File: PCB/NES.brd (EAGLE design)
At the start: 58.5 x 61 mm, 15 parts, among them U1 SN74AHCT125N, U2 SN74AHCT125N

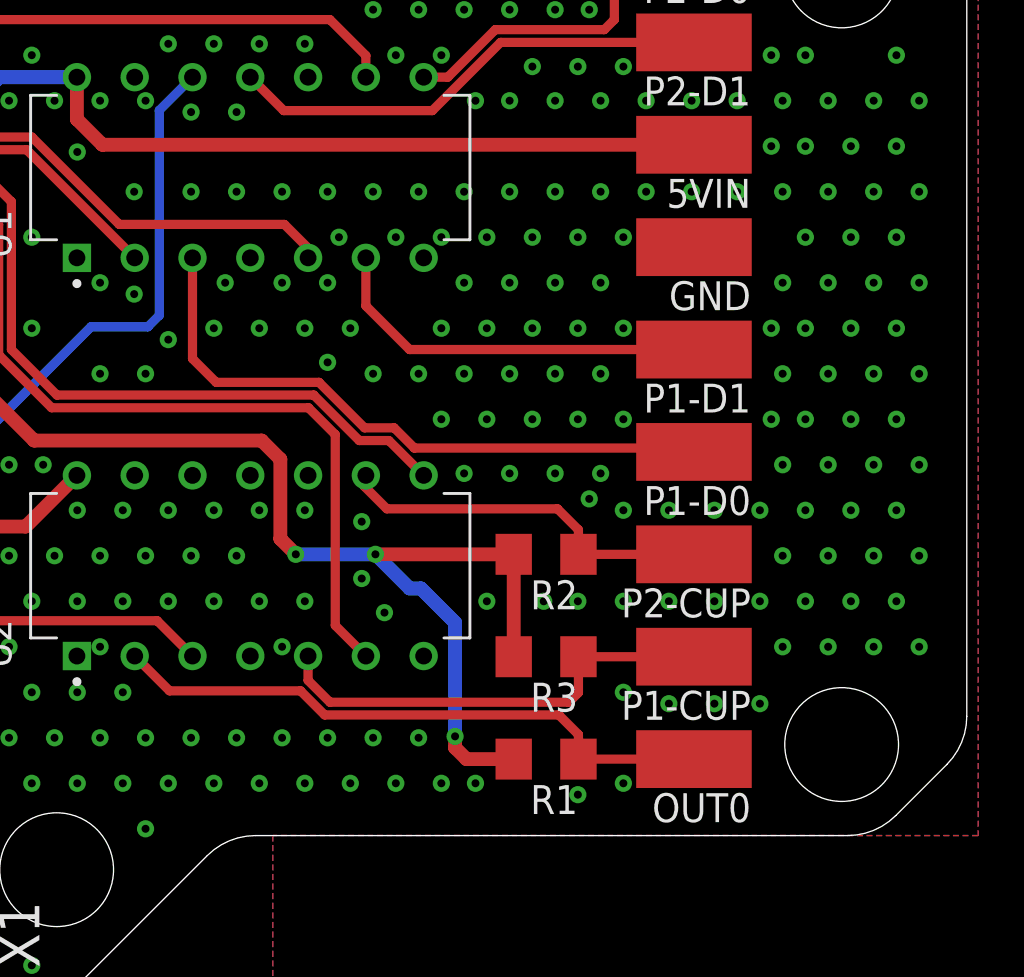
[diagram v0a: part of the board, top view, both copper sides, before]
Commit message: PCB Updates/New Additions
All existing PCBs had silkscreen updates and NES, Virtual Boy, PSX/PS2, Nintendo 64, Saturn have been added.
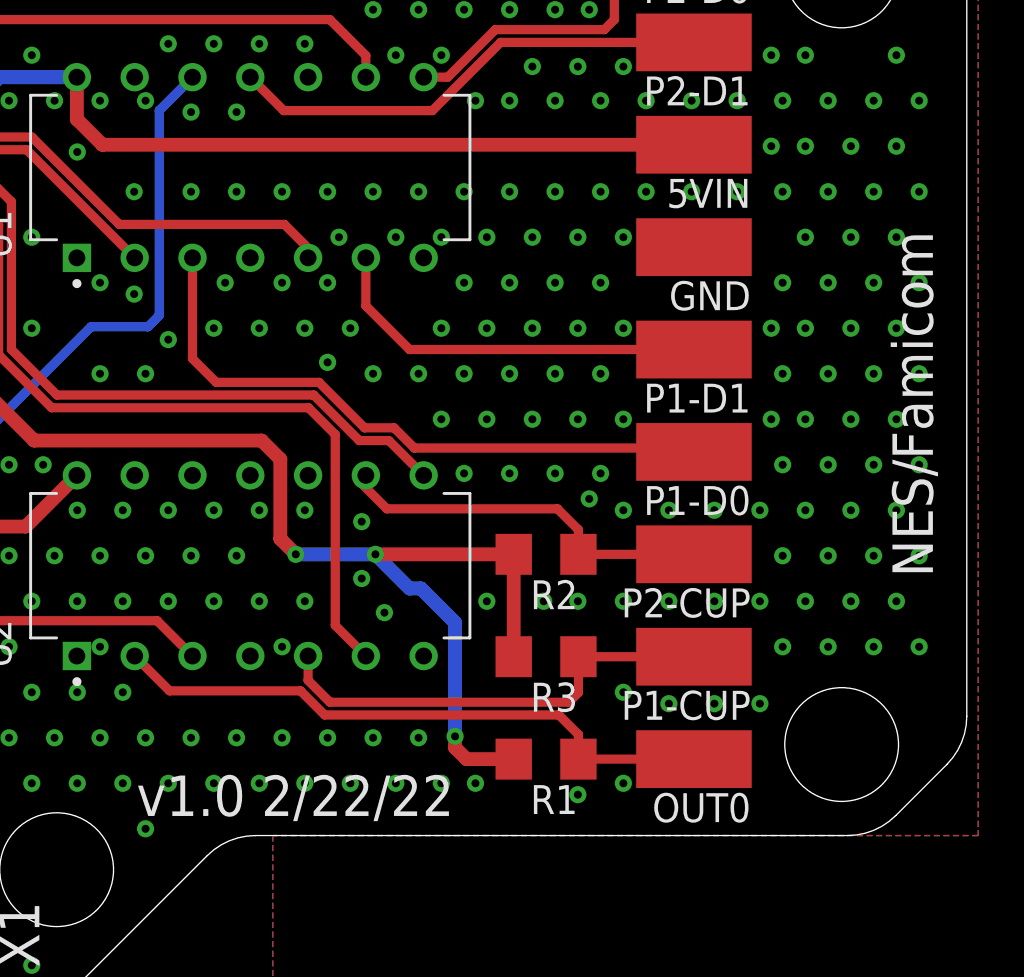
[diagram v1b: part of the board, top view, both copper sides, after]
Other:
- board text added: "NES/Famicom"
- board text added: "v1.0 2/22/22"
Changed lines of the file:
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@@
 <drawing>
 <settings>
-<setting alwaysvectorfont="yes"/>
+<setting alwaysvectorfont="no"/>
 <setting verticaltext="up"/>
 </settings>
@@
 <hole x="18.49" y="53.14" drill="5"/>
 <hole x="18.49" y="8.14" drill="5"/>
+<text x="57" y="21" size="1.778" layer="21" rot="R90">NES/Famicom</text>
+<text x="22" y="10.5" size="1.778" layer="21">v1.0 2/22/22</text>
 </plain>
 <attributes>
@@
 <element name="R1" library="adafruit" library_urn="urn:adsk.eagle:library:420" package="R1206" package3d_urn="urn:adsk.eagle:package:6240569/1" value="3.6K" x="40" y="13" smashed="yes" rot="R180">
 <attribute name="NAME" x="41.397" y="11.857" size="1.27" layer="25" rot="R180"/>
-<attribute name="VALUE" x="41.397" y="15.413" size="1.27" layer="27" rot="R180"/>
 </element>
 <element name="R2" library="adafruit" library_urn="urn:adsk.eagle:library:420" package="R1206" package3d_urn="urn:adsk.eagle:package:6240569/1" value="3.6K" x="40" y="22" smashed="yes" rot="R180">
 <attribute name="NAME" x="41.397" y="20.857" size="1.27" layer="25" rot="R180"/>
-<attribute name="VALUE" x="41.397" y="24.413" size="1.27" layer="27" rot="R180"/>
 </element>
 <element name="R3" library="adafruit" library_urn="urn:adsk.eagle:library:420" package="R1206" package3d_urn="urn:adsk.eagle:package:6240569/1" value="3.6K" x="40" y="17.5" smashed="yes" rot="R180">
 <attribute name="NAME" x="41.397" y="16.357" size="1.27" layer="25" rot="R180"/>
-<attribute name="VALUE" x="41.397" y="19.913" size="1.27" layer="27" rot="R180"/>
 </element>
 </elements>

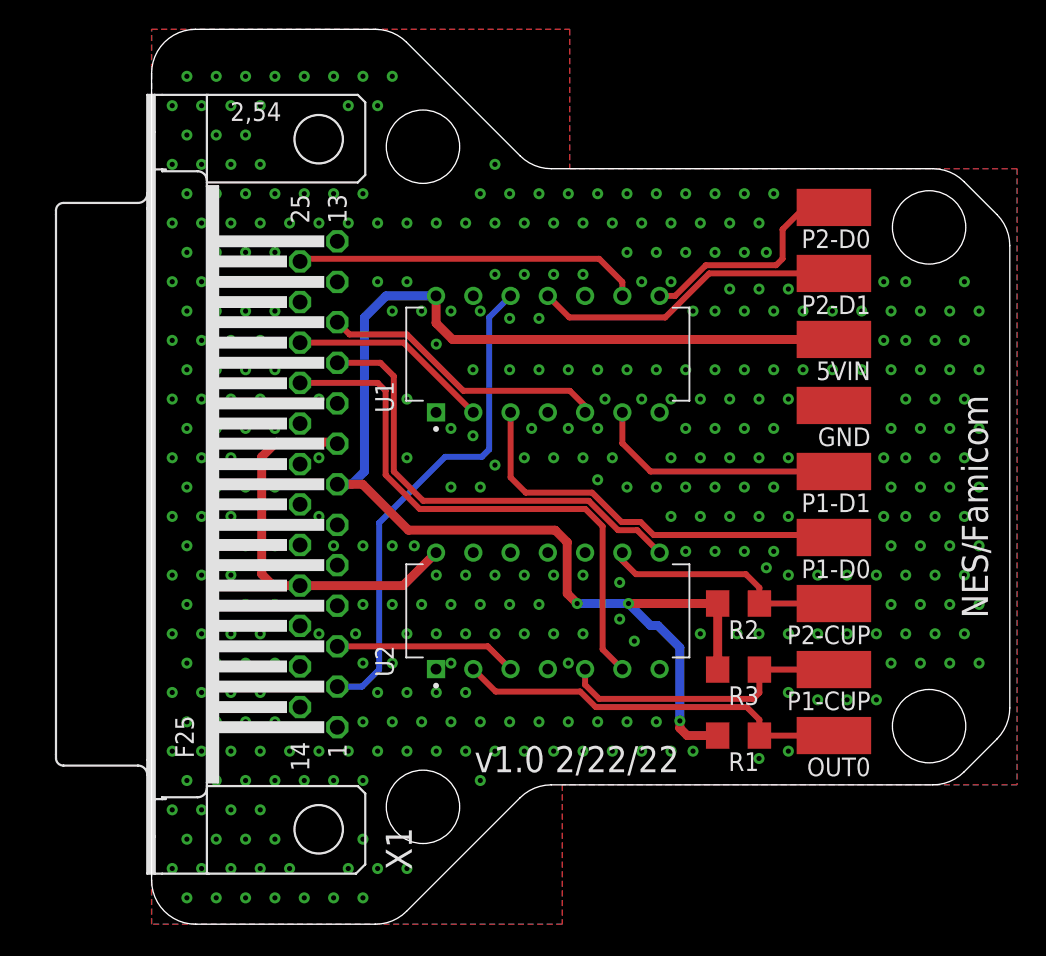
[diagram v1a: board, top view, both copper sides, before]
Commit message: PCB Update for better Housing Fit
All the PCBs were updated for better housing fitment.

Common Changes across all PCBs:
1. All Aux PCBs are now the exact same size.  (there was a .1mm-.5mm Variance previous)
2. All Aux PCBs Mounting holes are in the same location (there was a .05mm-.1mm Variance previous)
3. The DB25 has been moved 1.2mm close to the edge of the PCB for better connection when in the housing.

PCB Specific Updates:
3DO - Rename Pads (Removed trailing numbers), Flipped U2 to match U1, Moved U1 & U2 to same coordinates as other 2 Component PCBs in collection.

PCE & NES- Moved U1 & U2 to same coordinates as other 2 Component PCBs in collection.

PS2/PSX & Saturn - Added Notch on back edge of PCB for access for wires that need to attach to bottom layer of PCB.

All Gerbers have been updated.

New PCBs have been ordered for testing.
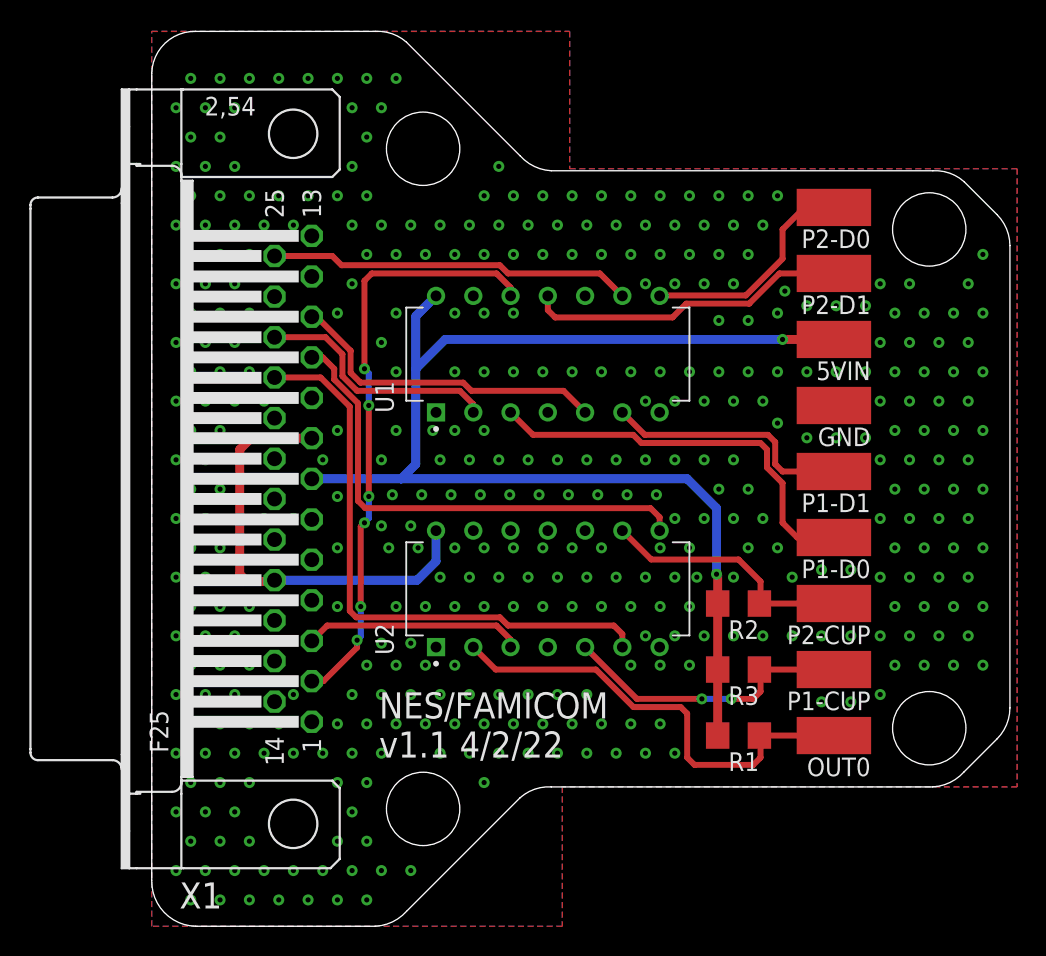
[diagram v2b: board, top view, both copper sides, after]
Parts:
- moved X1 1.78 mm to (9.64, 30.5)
- moved U2 1.50 mm to (27.0, 23.0)
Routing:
- net 5VIN: track 96.5 -> 86.7 mm, vias 3 -> 2
- net IO25: track 34.0 -> 40.6 mm, vias 0 -> 6
- net OUT0: track 27.1 -> 31.5 mm
- net 3V3IN: track 26.7 -> 30.0 mm
- net IO19: track 13.8 -> 16.9 mm
- net IO21: track 19.7 -> 22.2 mm
- net IO32: track 12.5 -> 14.9 mm
- net IO18: track 31.1 -> 33.5 mm
- net IO5: track 38.3 -> 40.0 mm
- net IO22: track 23.6 -> 24.8 mm
- net P2-D1: track 21.4 -> 21.9 mm
- net P2-CUP: track 16.9 -> 17.4 mm
- net P1-CUP: vias 0 -> 2
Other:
- outline, holes or cut-outs redrawn
- board text added: "NES/FAMICOM v1.1 4/2/22"
- board text removed: "NES/Famicom"
- board text removed: "v1.0 2/22/22"

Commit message: Added exposed GND plane at DB25 anchors
All PCBs have been update to have exposed GND plane pads for the DB25 anchor points.

This resolves Issue 54
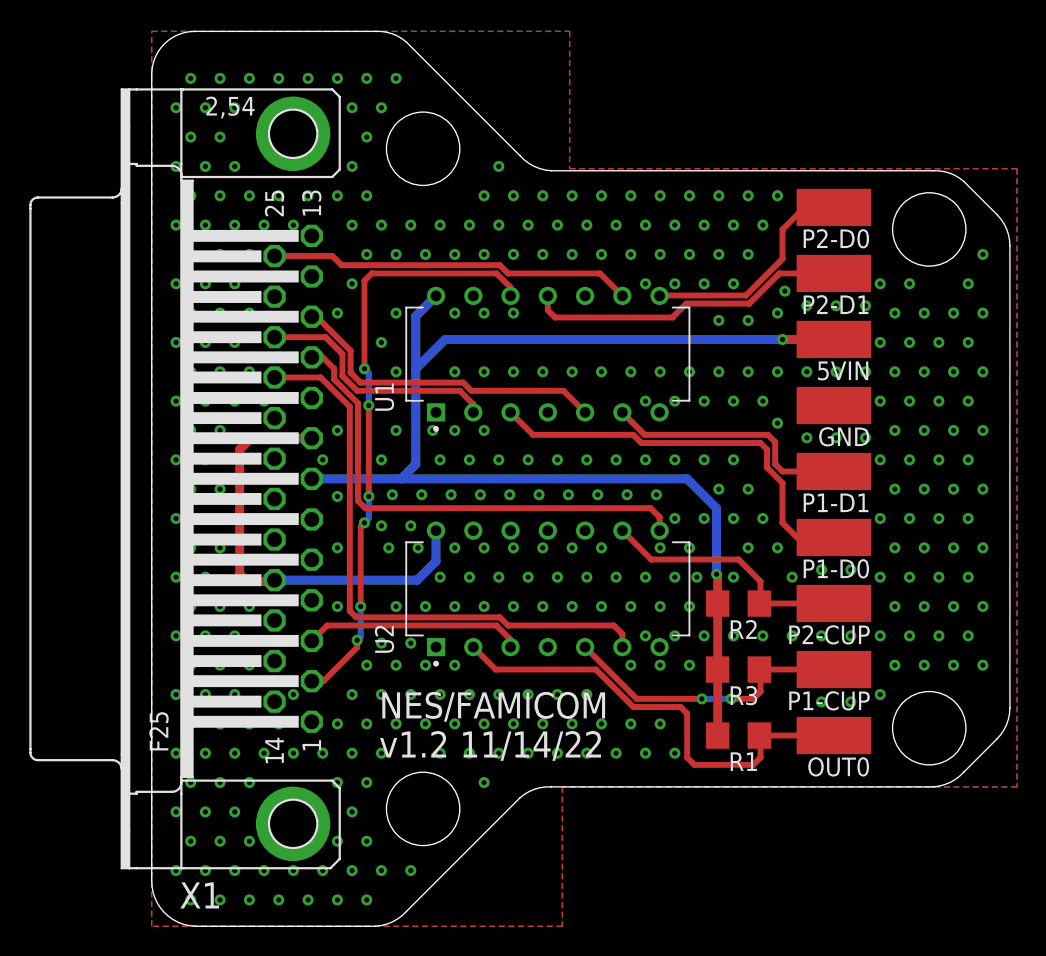
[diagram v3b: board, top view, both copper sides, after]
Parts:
- X1: device SparkFun-Retired:F25H -> SparkFun-Retired:F25HP
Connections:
- net GND: now also X1.GND1, X1.GND2
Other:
- board text added: "NES/FAMICOM v1.2 11/14/22"
- board text removed: "NES/FAMICOM v1.1 4/2/22"
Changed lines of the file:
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@@
 <hole x="18.5" y="8" drill="5"/>
 <text x="15.5" y="11.5" size="1.778" layer="21">NES/FAMICOM
-v1.1 4/2/22</text>
+v1.2 11/14/22</text>
 </plain>
 <attributes>
@@
 <attribute name="PURCHASE-URL" value="https://pricing.snapeda.com/search/part/SN74AHCT125N/?ref=eda" x="65.1" y="47.13" size="1.778" layer="27" rot="R90" display="off"/>
 </element>
-<element name="X1" library="SparkFun-Retired" package="F25H" value="" x="9.64" y="30.5" smashed="yes" rot="R90">
+<element name="X1" library="SparkFun-Retired" package="F25HP" value="" x="9.64" y="30.5" smashed="yes" rot="R90">
 <attribute name="NAME" x="4.789" y="2.99" size="1.778" layer="25" ratio="10" rot="R180"/>
 <attribute name="VALUE" x="-4.33" y="22.118" size="1.778" layer="27" ratio="10" rot="R90"/>
@@
 <via x="55.6568" y="43.7968" extent="1-16" drill="0.35"/>
 <via x="56.6568" y="45.7968" extent="1-16" drill="0.35"/>
+<contactref element="X1" pad="GND1"/>
+<contactref element="X1" pad="GND2"/>
 </signal>
 <signal name="5VIN">

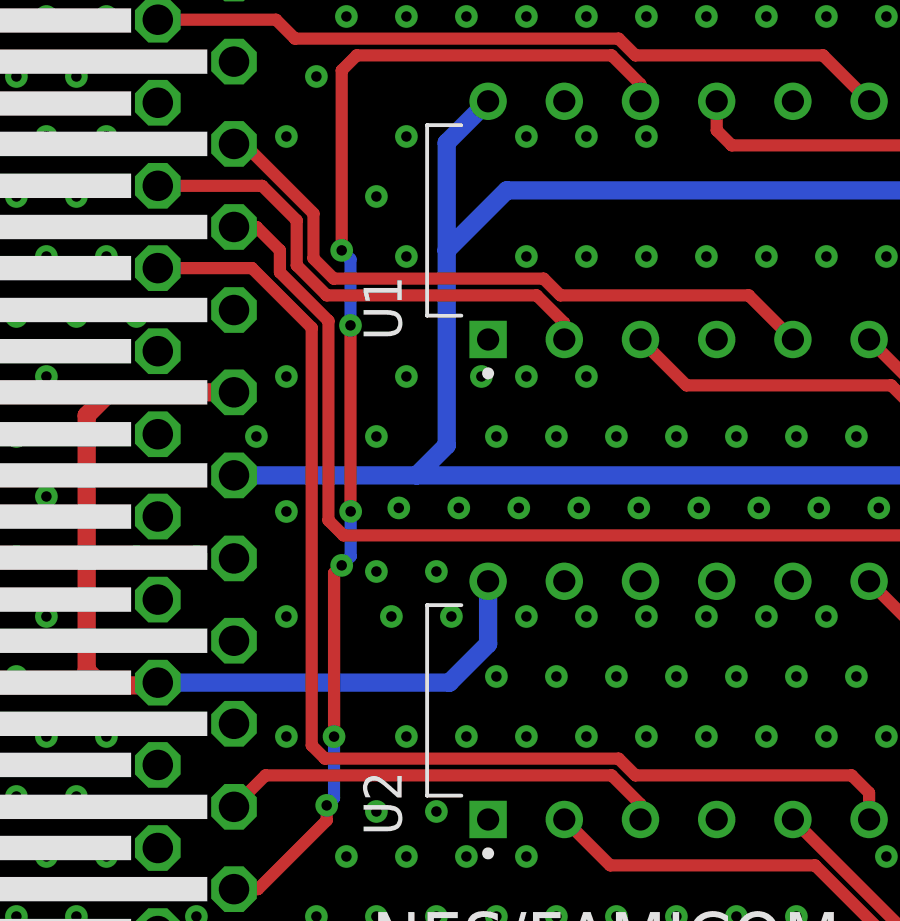
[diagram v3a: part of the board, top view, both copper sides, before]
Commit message: Silkscreen Update, Library Add, Datasheet Add
Updated the silkscreen on all PCBs that used the SN74 components as there was not orientation marker on the silkscreen.

Added Modified SN74 libraries and VB Cable Pinout image
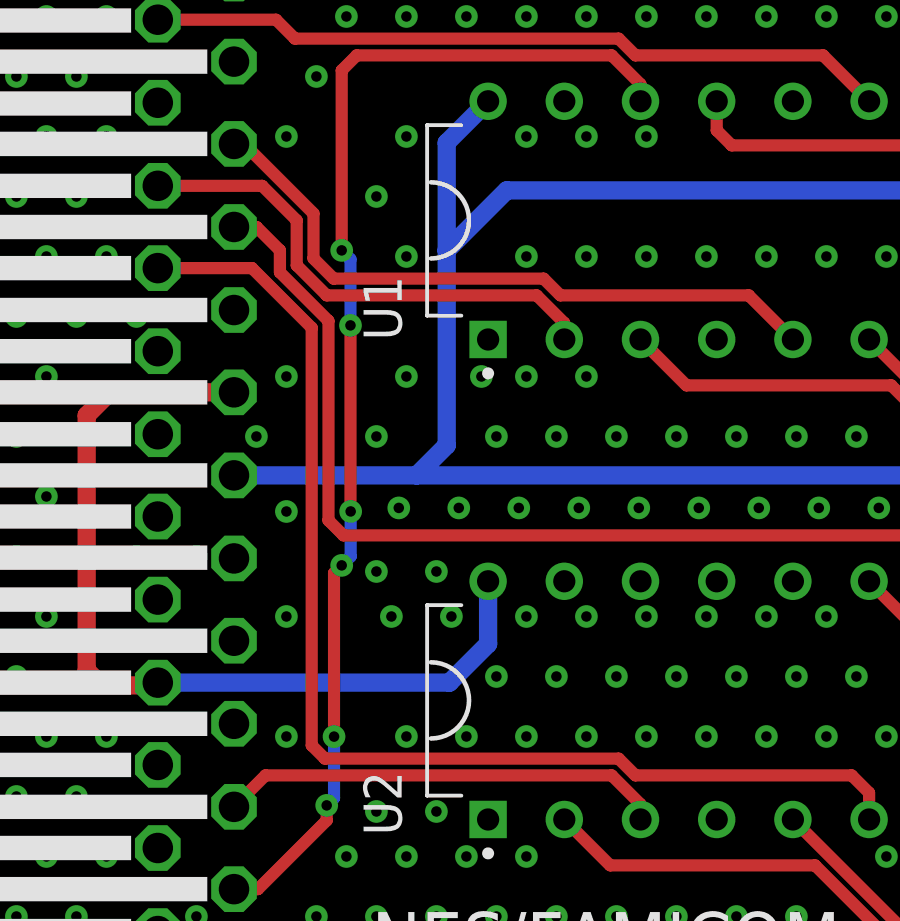
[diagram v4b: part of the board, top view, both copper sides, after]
